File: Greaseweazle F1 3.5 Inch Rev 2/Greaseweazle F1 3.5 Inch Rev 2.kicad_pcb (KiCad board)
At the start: 2 copper layers, 170.2 x 100 mm, 67 parts, among them CN1 Floppy Data, J1 USB B, J10 Conn_01x03, J11 Conn_01x03, J12 Display Port, J13 Display Port, J2 USB Header, J3 Floppy Power, J4 Floppy Power Header, J5 Programming Port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

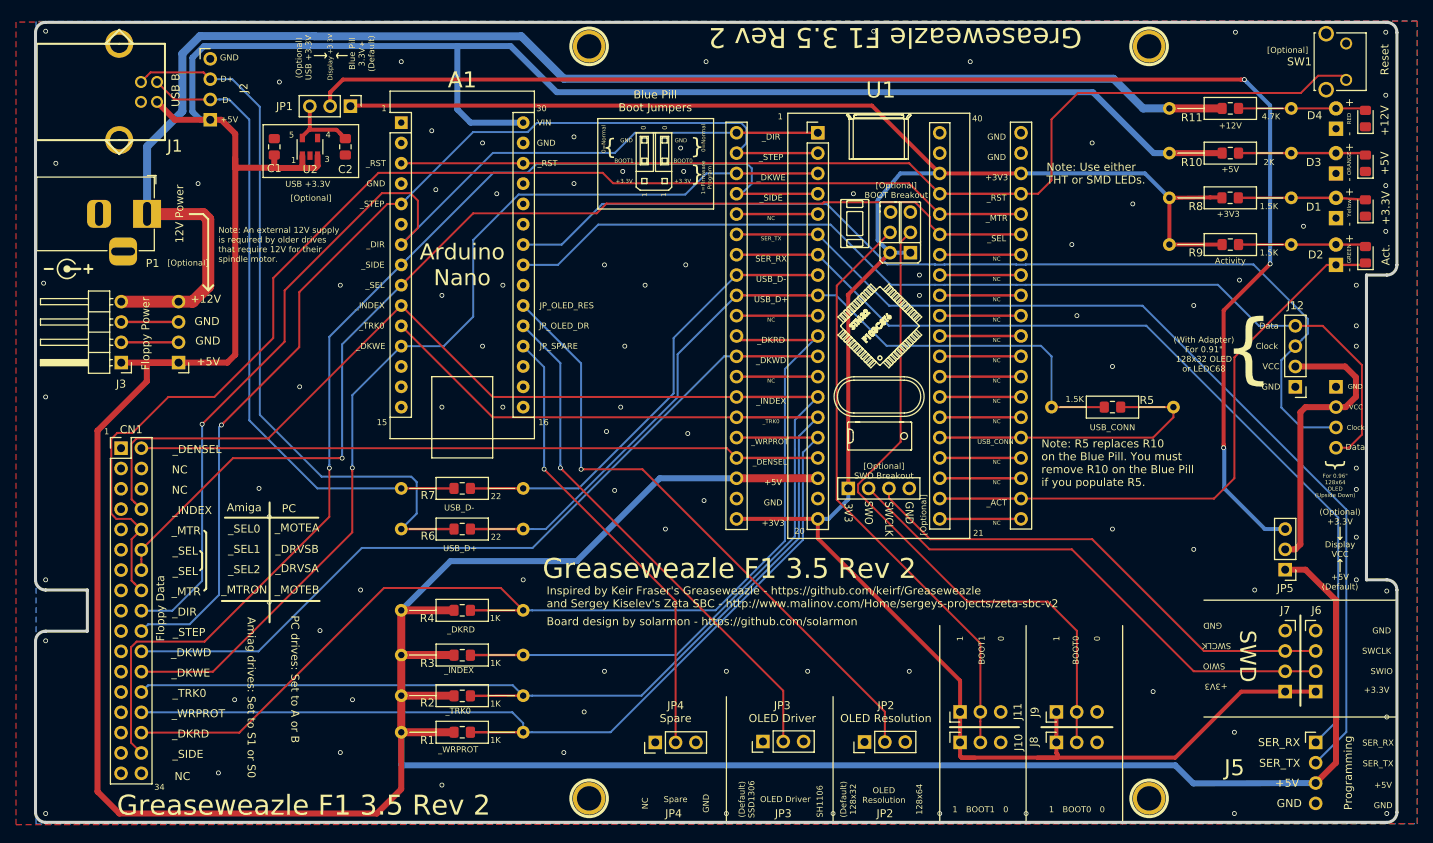
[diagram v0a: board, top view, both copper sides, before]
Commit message: Added Bumpon 3D model
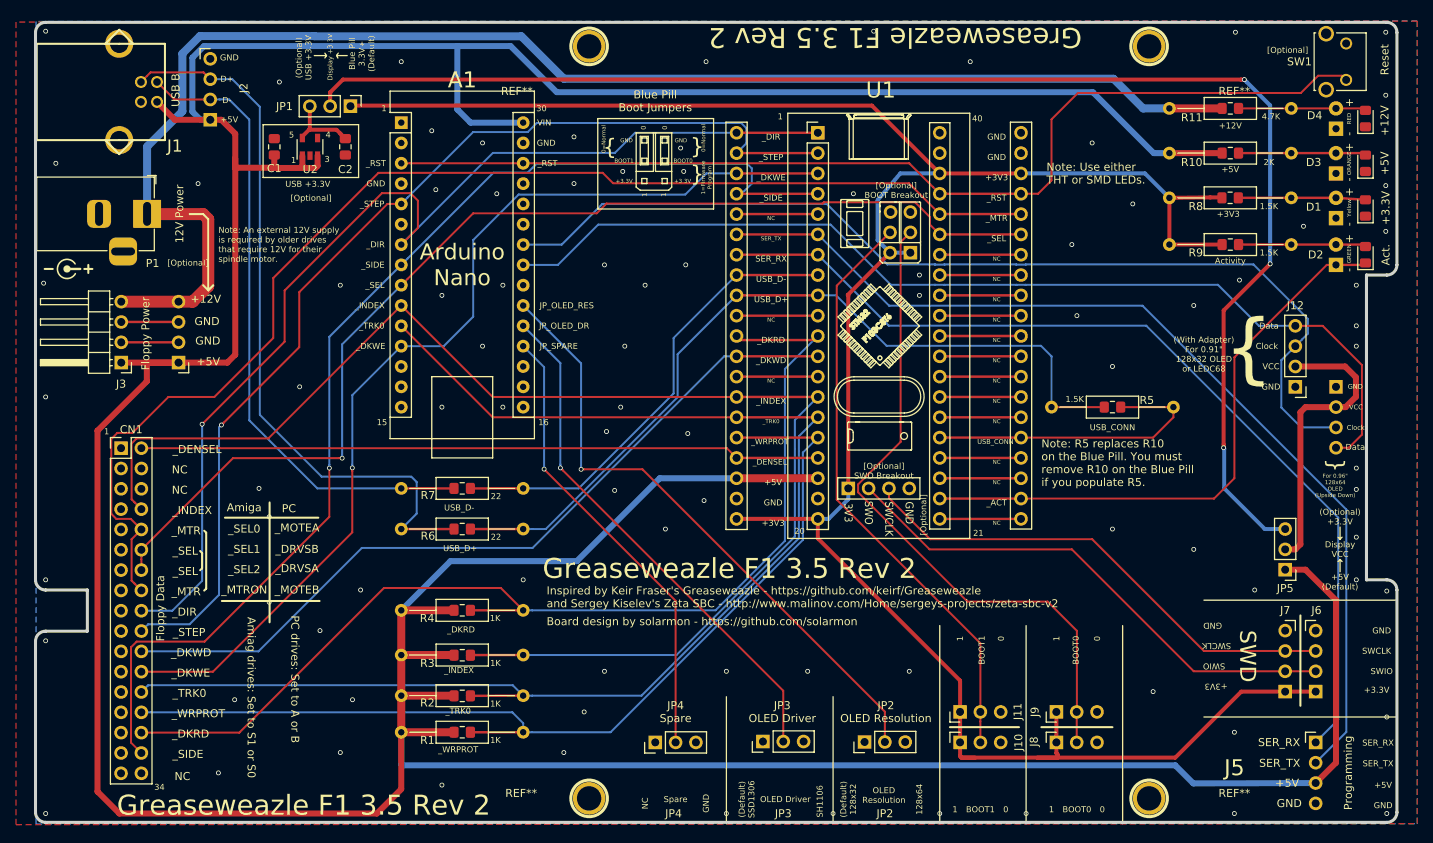
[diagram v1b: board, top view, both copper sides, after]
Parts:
- added REF**: Bumpon, solarmon_library:Bumpon, F.Cu at (111.0, 57.0)
- added REF**: Bumpon, solarmon_library:Bumpon, F.Cu at (200.7, 57.0)
- added REF**: Bumpon, solarmon_library:Bumpon, F.Cu at (200.7, 144.8)
- added REF**: Bumpon, solarmon_library:Bumpon, F.Cu at (111.5, 144.8)
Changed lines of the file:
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@@
     (tracks 643)
     (zones 0)
-    (modules 67)
+    (modules 71)
     (nets 77)
   )
@@
     (add_net /Display_VCC)
   )
+  (module solarmon_library:Bumpon (layer F.Cu)
+    (at 110.9726 57.023)
+    (fp_text reference REF** (at 0 2.54) (layer F.SilkS)
+      (effects (font (size 1 1) (thickness 0.15)))
+    )
+    (fp_text value Bumpon (at 0 -2.032) (layer F.Fab)
+      (effects (font (size 1 1) (thickness 0.15)))
+    )
+    (fp_circle (center 0 0) (end 0.762 0.762) (layer Dwgs.User) (width 0.12))
+    (model "${KISYS3DMOD}/bumpon-sj5508-1.snapshot.2/Bumpon (SJ5508).STEP"
+      (offset (xyz 0 0 -1.75))
+      (scale (xyz 1 1 1))
+      (rotate (xyz 90 0 0))
+    )
+  )
+  (module solarmon_library:Bumpon (layer F.Cu)
+    (at 200.66 57.023)
+    (fp_text reference REF** (at 0 2.54) (layer F.SilkS)
+      (effects (font (size 1 1) (thickness 0.15)))
+    )
+    (fp_text value Bumpon (at 0 -2.032) (layer F.Fab)
+      (effects (font (size 1 1) (thickness 0.15)))
+    )
+    (fp_circle (center 0 0) (end 0.762 0.762) (layer Dwgs.User) (width 0.12))
+    (model "${KISYS3DMOD}/bumpon-sj5508-1.snapshot.2/Bumpon (SJ5508).STEP"
+      (offset (xyz 0 0 -1.75))
+      (scale (xyz 1 1 1))
+      (rotate (xyz 90 0 0))
+    )
+  )
+  (module solarmon_library:Bumpon (layer F.Cu)
+    (at 200.66 144.78)
+    (fp_text reference REF** (at 0 2.54) (layer F.SilkS)
+      (effects (font (size 1 1) (thickness 0.15)))
+    )
+    (fp_text value Bumpon (at 0 -2.032) (layer F.Fab)
+      (effects (font (size 1 1) (thickness 0.15)))
+    )
+    (fp_circle (center 0 0) (end 0.762 0.762) (layer Dwgs.User) (width 0.12))
+    (model "${KISYS3DMOD}/bumpon-sj5508-1.snapshot.2/Bumpon (SJ5508).STEP"
+      (offset (xyz 0 0 -1.75))
+      (scale (xyz 1 1 1))
+      (rotate (xyz 90 0 0))
+    )
+  )
+  (module solarmon_library:Bumpon (layer F.Cu)
+    (at 111.506 144.78)
+    (fp_text reference REF** (at 0 2.54) (layer F.SilkS)
+      (effects (font (size 1 1) (thickness 0.15)))
+    )
+    (fp_text value Bumpon (at 0 -2.032) (layer F.Fab)
+      (effects (font (size 1 1) (thickness 0.15)))
+    )
+    (fp_circle (center 0 0) (end 0.762 0.762) (layer Dwgs.User) (width 0.12))
+    (model "${KISYS3DMOD}/bumpon-sj5508-1.snapshot.2/Bumpon (SJ5508).STEP"
+      (offset (xyz 0 0 -1.75))
+      (scale (xyz 1 1 1))
+      (rotate (xyz 90 0 0))
+    )
+  )
   (module Module:Arduino_Nano (layer F.Cu)
